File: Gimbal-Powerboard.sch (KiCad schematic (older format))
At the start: 116 parts, among them Q1 Q_PMOS_DGS, Q2 Q_PMOS_DGS, Q3 R6020ENJSMD, Q4 R6020ENJSMD, Q5 R6020ENJSMD, Q6 R6020ENJSMD, Q7 R6020ENJSMD, Q8 R6020ENJSMD, U1 DRV8301, U2 NUP4201MR6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

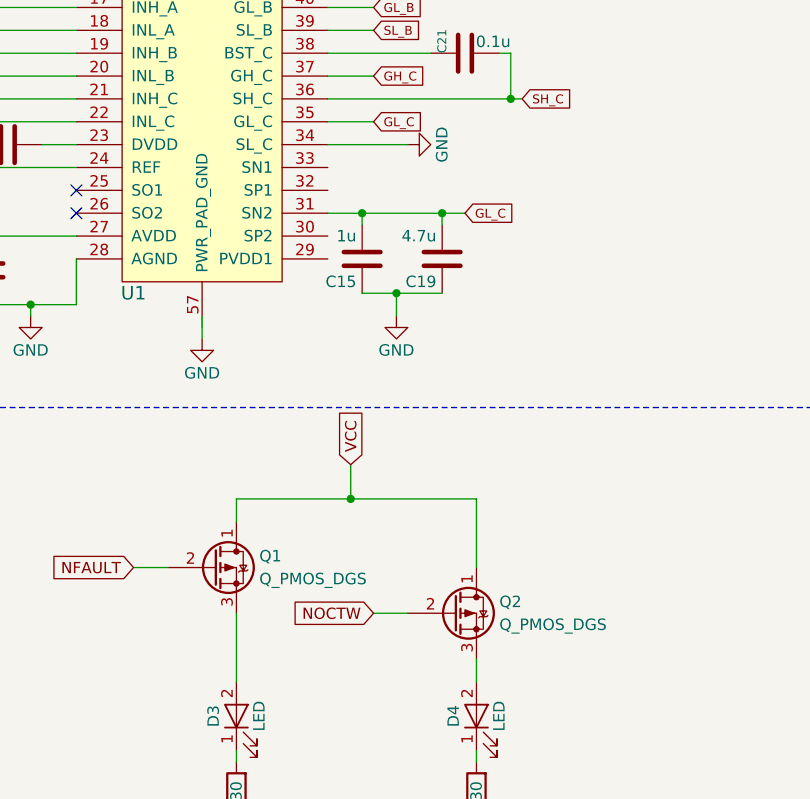
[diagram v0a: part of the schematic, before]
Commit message: Adjusted circuit implementation of DRV8301, adjusted FETs for LED indicators to have correct orientation for pads
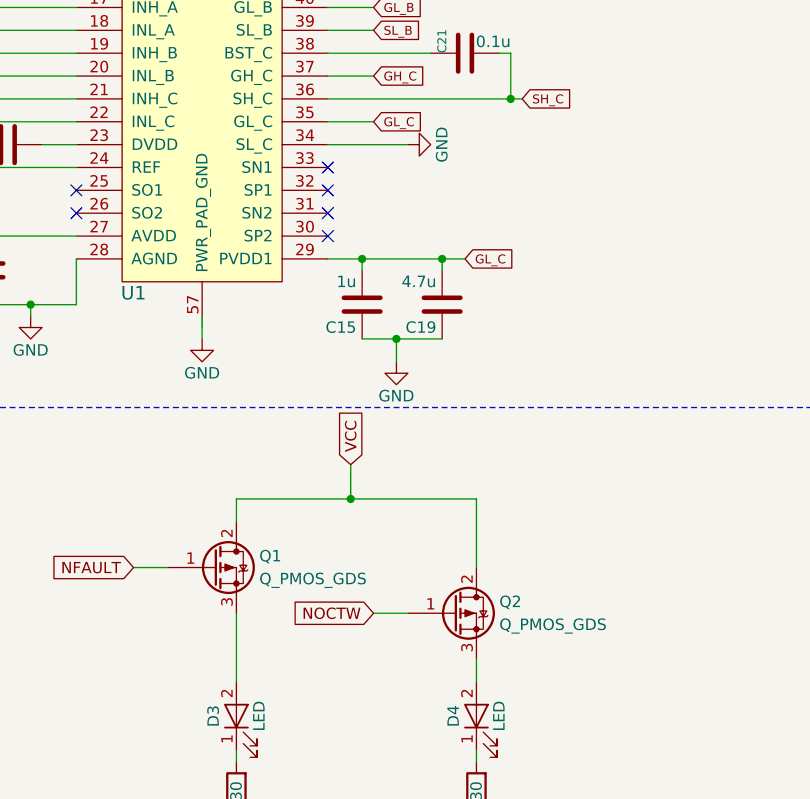
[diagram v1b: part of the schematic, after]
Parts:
- removed Q1, Q2: Q_PMOS_DGS, Diodes_SMD:D_SOT-23_ANK, symbol Q_PMOS_DGS
- added Q1, Q2: Q_PMOS_GDS, TO_SOT_Packages_SMD:SOT-23_Handsoldering, symbol Q_PMOS_GDS
- U4: footprint MRDT_ICs:SOIC-16_3.9x9.9mm_Pitch1.27mm -> MRDT_ICs:SOIC_16_3.9x9.9mm_Pitch1.27mm
- U5: footprint MRDT_Connectors:MOLEX_SL_3 -> MRDT_Connectors:MOLEX_SL_3_Horizontal
- U6: footprint MRDT_Connectors:MOLEX_SL_5 -> MRDT_Connectors:MOLEX_SL_5_Horizontal
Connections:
- net GL_C: now also U1.29 (PVDD1); no longer U1.31 (SN2)
- net NFAULT: now also Q1.1 (G)
- net NOCTW: now also Q2.1 (G)
- net VCC: now also Q1.2 (D), Q2.2 (D)
- net at D3.2 (A): now also Q1.3 (S)
- net at D4.2 (A): now also Q2.3 (S)
- no-connect marks 3 -> 7
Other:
- moved on the sheet: C15, C19
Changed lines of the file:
@@
 	1    0    0    -1
 $EndComp
-Text GLabel 8150 8050 2    39   Input ~ 0
+Text GLabel 8150 8250 2    39   Input ~ 0
 GL_C
 $Comp
 L C C15
 U 1 1 5A810D1B
-P 7700 8250
-F 0 "C15" H 7725 8350 50  0000 L CNN
-F 1 "1u" H 7725 8150 50  0000 L CNN
-F 2 "Capacitors_SMD:C_0805_HandSoldering" H 7738 8100 50  0001 C CNN
-F 3 "" H 7700 8250 50  0001 C CNN
-	1    7700 8250
+P 7700 8450
+F 0 "C15" H 7725 8550 50  0000 L CNN
+F 1 "1u" H 7725 8350 50  0000 L CNN
+F 2 "Capacitors_SMD:C_0805_HandSoldering" H 7738 8300 50  0001 C CNN
+F 3 "" H 7700 8450 50  0001 C CNN
+	1    7700 8450
 	-1   0    0    1
 $EndComp
@@
 L C C19
 U 1 1 5A810DF5
-P 8050 8250
-F 0 "C19" H 8075 8350 50  0000 L CNN
-F 1 "4.7u" H 8075 8150 50  0000 L CNN
-F 2 "Capacitors_SMD:C_1206_HandSoldering" H 8088 8100 50  0001 C CNN
-F 3 "" H 8050 8250 50  0001 C CNN
-	1    8050 8250
+P 8050 8450
+F 0 "C19" H 8075 8550 50  0000 L CNN
+F 1 "4.7u" H 8075 8350 50  0000 L CNN
+F 2 "Capacitors_SMD:C_1206_HandSoldering" H 8088 8300 50  0001 C CNN
+F 3 "" H 8050 8450 50  0001 C CNN
+	1    8050 8450
 	-1   0    0    1
 $EndComp
@@
 L GND #PWR020
 U 1 1 5A8114A2
-P 7850 8500
-F 0 "#PWR020" H 7850 8250 50  0001 C CNN
-F 1 "GND" H 7850 8350 50  0000 C CNN
-F 2 "" H 7850 8500 50  0001 C CNN
-F 3 "" H 7850 8500 50  0001 C CNN
-	1    7850 8500
+P 7850 8700
+F 0 "#PWR020" H 7850 8450 50  0001 C CNN
+F 1 "GND" H 7850 8550 50  0000 C CNN
+F 2 "" H 7850 8700 50  0001 C CNN
+F 3 "" H 7850 8700 50  0001 C CNN
+	1    7850 8700
 	1    0    0    -1
 $EndComp
@@
 	1    0    0    -1
 $EndComp
-$Comp
-L Q_PMOS_DGS Q1
-U 1 1 5A8584F1
-P 7050 9600
-F 0 "Q1" H 7250 9650 50  0000 L CNN
-F 1 "Q_PMOS_DGS" H 7250 9550 50  0000 L CNN
-F 2 "Diodes_SMD:D_SOT-23_ANK" H 7250 9700 50  0001 C CNN
-F 3 "" H 7050 9600 50  0001 C CNN
-	1    7050 9600
-	1    0    0    -1
-$EndComp
 Text GLabel 6700 9600 0    49   Input ~ 0
 NFAULT
-$Comp
-L Q_PMOS_DGS Q2
-U 1 1 5A858CF9
-P 8100 9800
-F 0 "Q2" H 8300 9850 50  0000 L CNN
-F 1 "Q_PMOS_DGS" H 8300 9750 50  0000 L CNN
-F 2 "Diodes_SMD:D_SOT-23_ANK" H 8300 9900 50  0001 C CNN
-F 3 "" H 8100 9800 50  0001 C CNN
-	1    8100 9800
-	1    0    0    -1
-$EndComp
 Text GLabel 7750 9800 0    49   Input ~ 0
 NOCTW
@@
 F 0 "U4" H 17050 11025 50  0000 R CNN
 F 1 "MAX3232" H 17050 10950 50  0000 R CNN
-F 2 "MRDT_ICs:SOIC-16_3.9x9.9mm_Pitch1.27mm" H 17200 8850 50  0001 L CNN
+F 2 "MRDT_ICs:SOIC_16_3.9x9.9mm_Pitch1.27mm" H 17200 8850 50  0001 L CNN
 F 3 "" H 17150 10000 50  0001 C CNN
 	1    17150 9900
@@
 F 0 "U6" H 18850 4200 60  0001 C CNN
 F 1 "Molex_SL-5" H 19000 4800 60  0000 C CNN
-F 2 "MRDT_Connectors:MOLEX_SL_5" H 18800 4250 60  0001 C CNN
+F 2 "MRDT_Connectors:MOLEX_SL_5_Horizontal" H 18800 4250 60  0001 C CNN
 F 3 "" H 18800 4250 60  0001 C CNN
 	1    18800 4250
@@
 F 0 "U5" H 18850 3100 60  0001 C CNN
 F 1 "Molex_SL-3" H 19000 3500 60  0000 C CNN
-F 2 "MRDT_Connectors:MOLEX_SL_3" H 18800 3150 60  0001 C CNN
+F 2 "MRDT_Connectors:MOLEX_SL_3_Horizontal" H 18800 3150 60  0001 C CNN
 F 3 "" H 18800 3150 60  0001 C CNN
 	1    18800 3150
@@
 	7000 8500 7000 8600
 Wire Wire Line
-	7550 8050 8150 8050
-Wire Wire Line
-	7700 8050 7700 8100
-Connection ~ 7700 8050
-Wire Wire Line
-	7700 8400 8050 8400
-Wire Wire Line
-	8050 8100 8050 8050
-Connection ~ 8050 8050
-Wire Wire Line
-	7850 8400 7850 8500
-Connection ~ 7850 8400
+	7550 8250 8150 8250
+Wire Wire Line
+	7700 8250 7700 8300
+Connection ~ 7700 8250
+Wire Wire Line
+	7700 8600 8050 8600
+Wire Wire Line
+	8050 8300 8050 8250
+Connection ~ 8050 8250
+Wire Wire Line
+	7850 8600 7850 8700
+Connection ~ 7850 8600
 Wire Notes Line
 	3050 8900 10550 8900
@@
 	7650 6150 7650 6050
 Connection ~ 7650 6050
+$Comp
+L Q_PMOS_GDS Q1
+U 1 1 5AC277C8
+P 7050 9600
+F 0 "Q1" H 7250 9650 50  0000 L CNN
+F 1 "Q_PMOS_GDS" H 7250 9550 50  0000 L CNN
+F 2 "TO_SOT_Packages_SMD:SOT-23_Handsoldering" H 7250 9700 50  0001 C CNN
+F 3 "" H 7050 9600 50  0001 C CNN
+	1    7050 9600
+	1    0    0    -1
+$EndComp
+$Comp
+L Q_PMOS_GDS Q2
+U 1 1 5AC27BA4
+P 8100 9800
+F 0 "Q2" H 8300 9850 50  0000 L CNN
+F 1 "Q_PMOS_GDS" H 8300 9750 50  0000 L CNN
+F 2 "TO_SOT_Packages_SMD:SOT-23_Handsoldering" H 8300 9900 50  0001 C CNN
+F 3 "" H 8100 9800 50  0001 C CNN
+	1    8100 9800
+	1    0    0    -1
+$EndComp
+NoConn ~ 7550 7850
+NoConn ~ 7550 7950
+NoConn ~ 7550 8050
+NoConn ~ 7550 8150
 $EndSCHEMATC
